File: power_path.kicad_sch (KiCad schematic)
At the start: 39 parts, among them J1 Battery, J2 USB_C_Receptacle_USB2.0_16P, SW1 MK-11C04-G013, U2 TPS631000DRLR, U3 TLV77018PDBVR, U4 TPS2116DRL, U5 USBLC6-2SC6, U6 USBLC6-2SC6, U7 BQ25302, U8 BQ27427YZFR

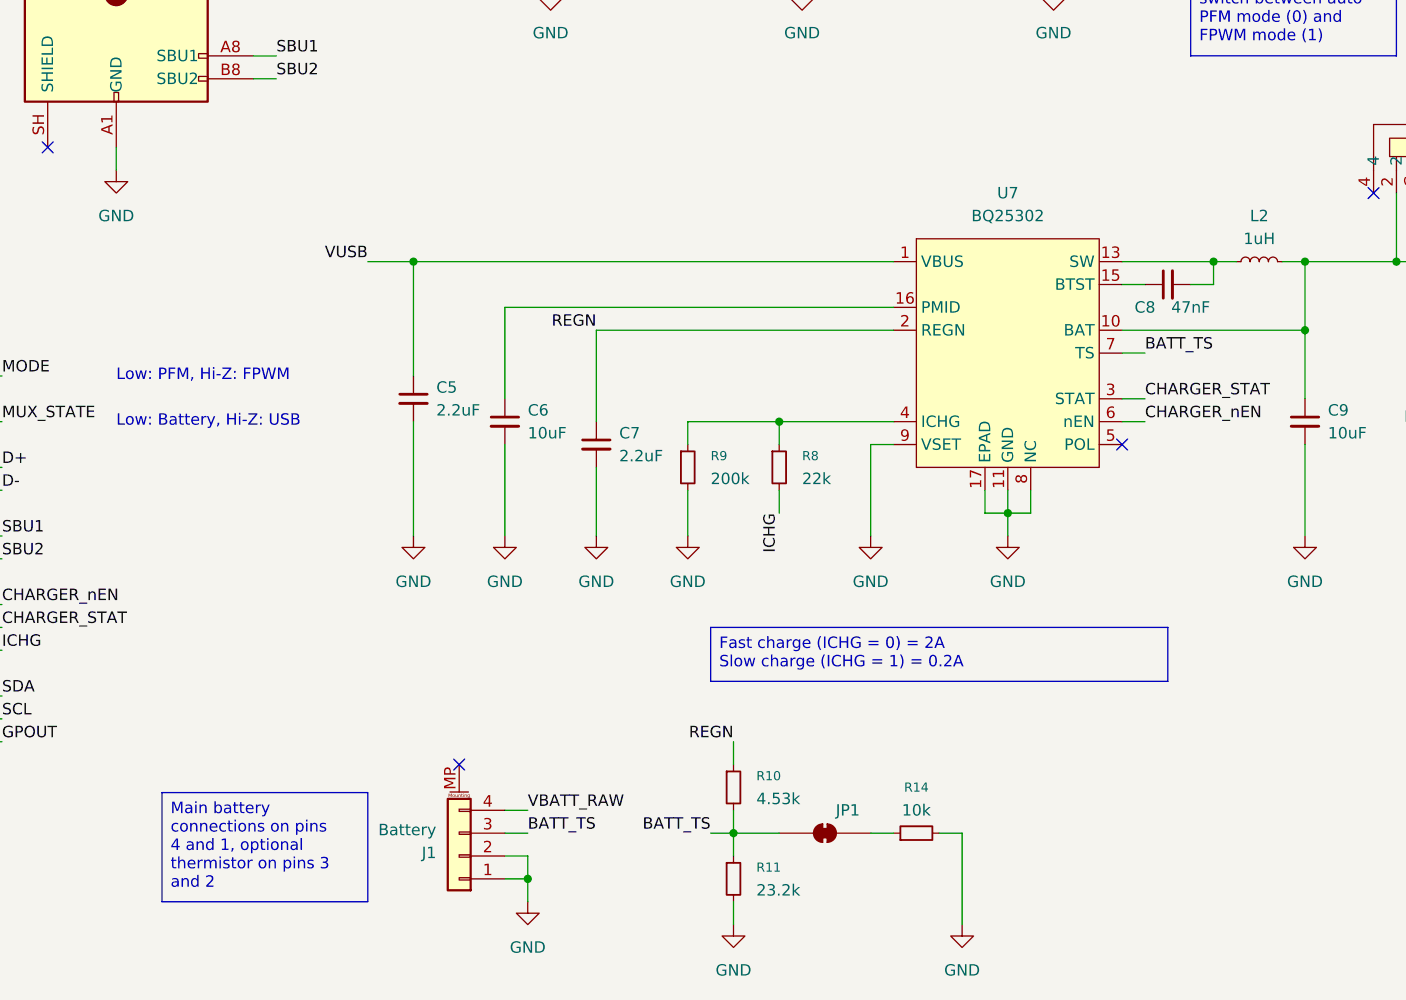
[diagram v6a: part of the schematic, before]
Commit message: add battery connector model and charge led
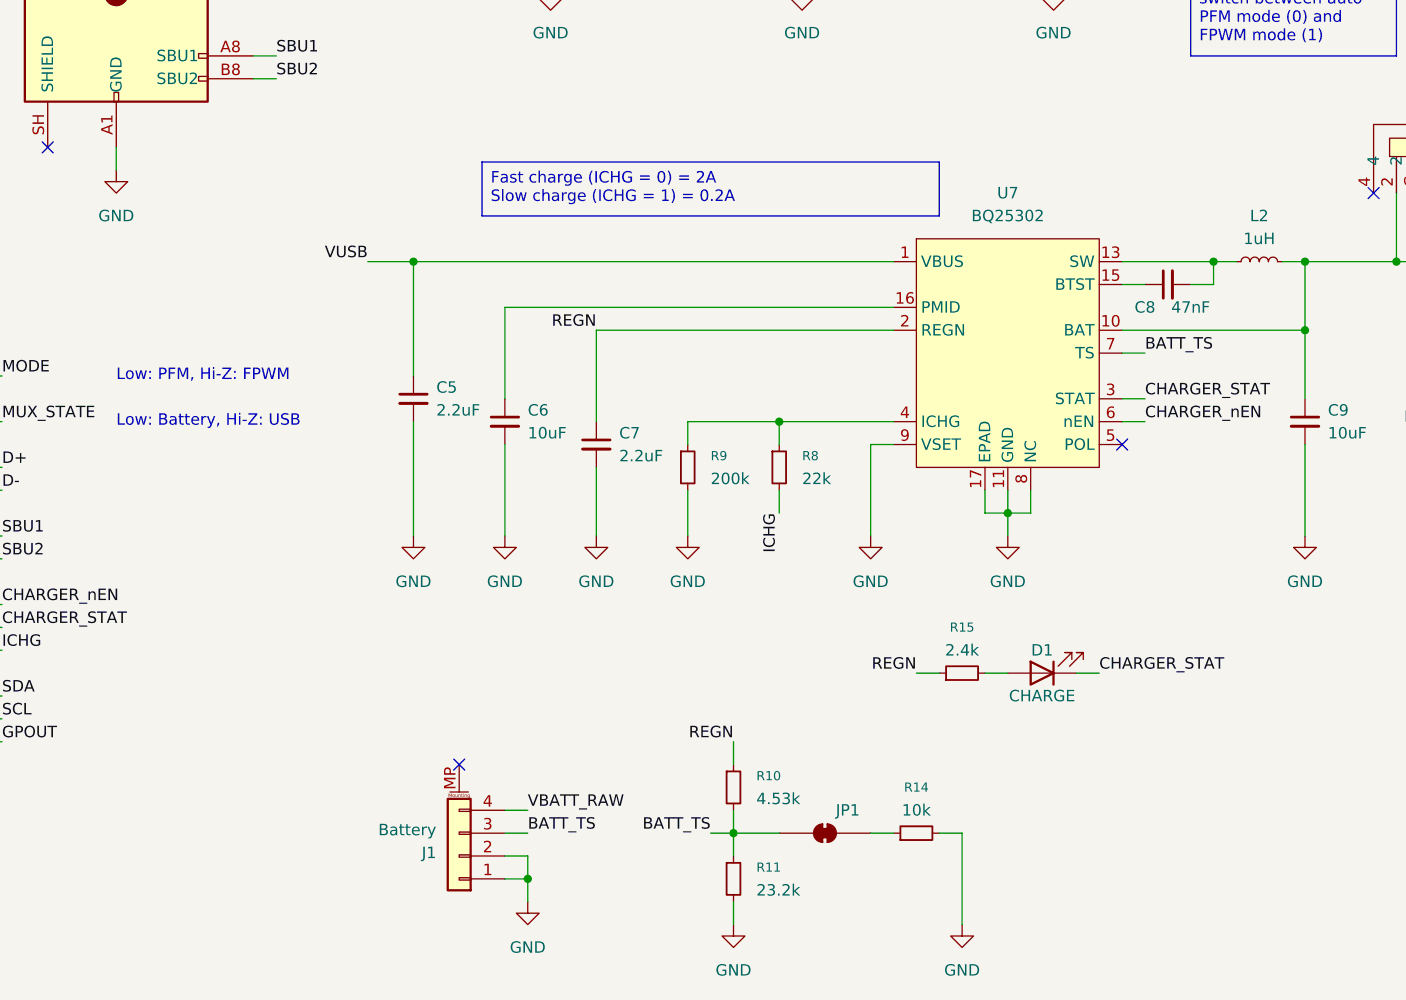
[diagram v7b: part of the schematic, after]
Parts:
- added D1: CHARGE, LED_SMD:LED_0402_1005Metric, symbol Device:LED
- added R15: 2.4k, Resistor_SMD:R_0402_1005Metric, symbol Device:R_Small
- J1: footprint (none) -> Connector_JST:JST_PH_S4B-PH-SM4-TB_1x04-1MP_P2.00mm_Horizontal; LCSC (none) -> C2763695
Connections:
- net CHARGER_STAT: now also D1.1 (K)
- net REGN: now also R15.1
- new net: D1.2 (A), R15.2

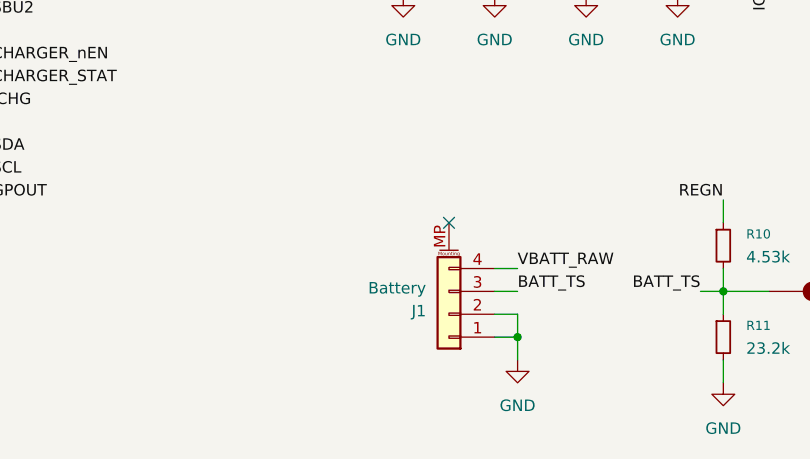
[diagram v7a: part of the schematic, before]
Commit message: replace battery connector with solder pads
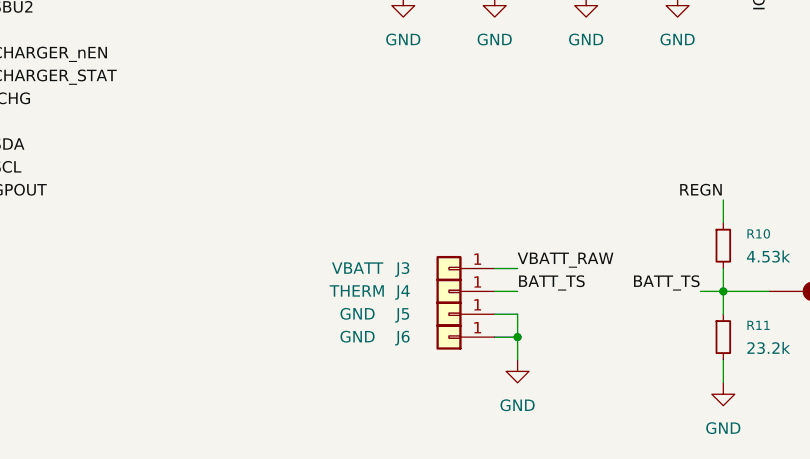
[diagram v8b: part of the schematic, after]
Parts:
- removed J1: Battery, Connector_JST:JST_PH_S4B-PH-SM4-TB_1x04-1MP_P2.00mm_Horizontal, symbol Connector_Generic_MountingPin:Conn_01x04_MountingPin
- added J3: VBATT, Connector_Wire:SolderWirePad_1x01_SMD_1x2mm, symbol Connector_Generic:Conn_01x01
- added J4: THERM, Connector_Wire:SolderWirePad_1x01_SMD_1x2mm, symbol Connector_Generic:Conn_01x01
- added J5, J6: GND, Connector_Wire:SolderWirePad_1x01_SMD_1x2mm, symbol Connector_Generic:Conn_01x01
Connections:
- net BATT_TS: now also J4.1 (Pin_1)
- net GND: now also J5.1 (Pin_1), J6.1 (Pin_1)
- net VBATT_RAW: now also J3.1 (Pin_1)
- no-connect marks 6 -> 5
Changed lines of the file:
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@@
 	)
 	(no_connect
-		(at 88.9 170.18)
-	)
-	(no_connect
 		(at 198.12 106.68)
 	)
@@
 	)
 	(symbol
+		(lib_id "Connector_Generic:Conn_01x01")
+		(at 88.9 177.8 180)
+		(unit 1)
+		(body_style 1)
+		(exclude_from_sim no)
+		(in_bom yes)
+		(on_board yes)
+		(in_pos_files yes)
+		(dnp no)
+		(property "Reference" "J4"
+			(at 83.82 177.8 0)
+			(show_name no)
+			(do_not_autoplace no)
+			(effects
+				(font
+					(size 1.27 1.27)
+				)
+			)
+		)
+		(property "Value" "THERM"
+			(at 78.74 177.8 0)
+			(show_name no)
+			(do_not_autoplace no)
+			(effects
+				(font
+					(size 1.27 1.27)
+				)
+			)
+		)
+		(property "Footprint" "Connector_Wire:SolderWirePad_1x01_SMD_1x2mm"
+			(at 88.9 177.8 0)
+			(hide yes)
+			(show_name no)
+			(do_not_autoplace no)
+			(effects
+				(font
+					(size 1.27 1.27)
+				)
+			)
+		)
+		(property "Datasheet" ""
+			(at 88.9 177.8 0)
+			(hide yes)
+			(show_name no)
+			(do_not_autoplace no)
+			(effects
+				(font
+					(size 1.27 1.27)
+				)
+			)
+		)
+		(property "Description" "Generic connector, single row, 01x01, script generated (kicad-library-utils/schlib/autogen/connector/)"
+			(at 88.9 177.8 0)
+			(hide yes)
+			(show_name no)
+			(do_not_autoplace no)
+			(effects
+				(font
+					(size 1.27 1.27)
+				)
+			)
+		)
+		(pin "1"
+		)
+		(instances
+			(project "pedal"
+				(path "/e2443317-b83f-4e66-ac79-3186c6d613f3/487ab5a8-1c1d-4a3e-8f62-a21afc38e9a3"
+					(reference "J4")
+					(unit 1)
+				)
+			)
+		)
+	)
+	(symbol
 		(lib_id "power:GND")
 		(at 96.52 185.42 0)
@@
 	)
 	(symbol
-		(lib_id "Connector_Generic_MountingPin:Conn_01x04_MountingPin")
-		(at 88.9 180.34 180)
+		(lib_id "Device:R_Small")
+		(at 71.12 71.12 90)
 		(unit 1)
 		(body_style 1)
@@
 		(in_pos_files yes)
 		(dnp no)
-		(fields_autoplaced yes)
-		(property "Reference" "J1"
-			(at 86.36 179.9845 0)
+		(property "Reference" "R7"
+			(at 68.58 73.66 90)
 			(show_name no)
 			(do_not_autoplace no)
 			(effects
 				(font
-					(size 1.27 1.27)
+					(size 1.016 1.016)
 				)
-				(justify left)
 			)
 		)
-		(property "Value" "Battery"
-			(at 86.36 177.4445 0)
+		(property "Value" "5.1k"
+			(at 73.66 73.66 90)
 			(show_name no)
 			(do_not_autoplace no)
@@
 					(size 1.27 1.27)
 				)
-				(justify left)
 			)
 		)
-		(property "Footprint" "Connector_JST:JST_PH_S4B-PH-SM4-TB_1x04-1MP_P2.00mm_Horizontal"
-			(at 88.9 180.34 0)
+		(property "Footprint" "Resistor_SMD:R_0402_1005Metric"
+			(at 71.12 71.12 0)
 			(hide yes)
 			(show_name no)
@@
 		)
 		(property "Datasheet" ""
-			(at 88.9 180.34 0)
+			(at 71.12 71.12 0)
 			(hide yes)
 			(show_name no)
@@
 			)
 		)
-		(property "Description" "Generic connectable mounting pin connector, single row, 01x04, script generated (kicad-library-utils/schlib/autogen/connector/)"
-			(at 88.9 180.34 0)
+		(property "Description" "Resistor, small symbol"
+			(at 71.12 71.12 0)
 			(hide yes)
 			(show_name no)
@@
 			)
 		)
-		(property "LCSC" "C2763695"
-			(at 88.9 180.34 0)
+		(property "LCSC" "C25905"
+			(at 71.12 71.12 0)
 			(hide yes)
 			(show_name no)
@@
 			)
 		)
-		(pin "2"
-		)
-		(pin "3"
-		)
-		(pin "MP"
-		)
-		(pin "4"
-		)
 		(pin "1"
 		)
+		(pin "2"
+		)
 		(instances
 			(project "pedal"
 				(path "/e2443317-b83f-4e66-ac79-3186c6d613f3/487ab5a8-1c1d-4a3e-8f62-a21afc38e9a3"
-					(reference "J1")
+					(reference "R7")
 					(unit 1)
 				)
@@
 	)
 	(symbol
-		(lib_id "Device:R_Small")
-		(at 71.12 71.12 90)
+		(lib_id "Connector_Generic:Conn_01x01")
+		(at 88.9 180.34 180)
 		(unit 1)
 		(body_style 1)
@@
 		(in_pos_files yes)
 		(dnp no)
-		(property "Reference" "R7"
-			(at 68.58 73.66 90)
-			(show_name no)
-			(do_not_autoplace no)
-			(effects
-				(font
-					(size 1.016 1.016)
-				)
-			)
-		)
-		(property "Value" "5.1k"
-			(at 73.66 73.66 90)
+		(property "Reference" "J5"
+			(at 83.82 180.34 0)
 			(show_name no)
 			(do_not_autoplace no)
@@
 			)
 		)
-		(property "Footprint" "Resistor_SMD:R_0402_1005Metric"
-			(at 71.12 71.12 0)
-			(hide yes)
+		(property "Value" "GND"
+			(at 78.74 180.34 0)
 			(show_name no)
 			(do_not_autoplace no)
@@
 			)
 		)
-		(property "Datasheet" ""
-			(at 71.12 71.12 0)
+		(property "Footprint" "Connector_Wire:SolderWirePad_1x01_SMD_1x2mm"
+			(at 88.9 180.34 0)
 			(hide yes)
 			(show_name no)
@@
 			)
 		)
-		(property "Description" "Resistor, small symbol"
-			(at 71.12 71.12 0)
+		(property "Datasheet" ""
+			(at 88.9 180.34 0)
 			(hide yes)
 			(show_name no)
@@
 			)
 		)
-		(property "LCSC" "C25905"
-			(at 71.12 71.12 0)
+		(property "Description" "Generic connector, single row, 01x01, script generated (kicad-library-utils/schlib/autogen/connector/)"
+			(at 88.9 180.34 0)
 			(hide yes)
 			(show_name no)
@@
 		(pin "1"
 		)
-		(pin "2"
-		)
 		(instances
 			(project "pedal"
 				(path "/e2443317-b83f-4e66-ac79-3186c6d613f3/487ab5a8-1c1d-4a3e-8f62-a21afc38e9a3"
-					(reference "R7")
+					(reference "J5")
 					(unit 1)
 				)
@@
 	)
 	(symbol
+		(lib_id "Connector_Generic:Conn_01x01")
+		(at 88.9 182.88 180)
+		(unit 1)
+		(body_style 1)
+		(exclude_from_sim no)
+		(in_bom yes)
+		(on_board yes)
+		(in_pos_files yes)
+		(dnp no)
+		(property "Reference" "J6"
+			(at 83.82 182.88 0)
+			(show_name no)
+			(do_not_autoplace no)
+			(effects
+				(font
+					(size 1.27 1.27)
+				)
+			)
+		)
+		(property "Value" "GND"
+			(at 78.74 182.88 0)
+			(show_name no)
+			(do_not_autoplace no)
+			(effects
+				(font
+					(size 1.27 1.27)
+				)
+			)
+		)
+		(property "Footprint" "Connector_Wire:SolderWirePad_1x01_SMD_1x2mm"
+			(at 88.9 182.88 0)
+			(hide yes)
+			(show_name no)
+			(do_not_autoplace no)
+			(effects
+				(font
+					(size 1.27 1.27)
+				)
+			)
+		)
+		(property "Datasheet" ""
+			(at 88.9 182.88 0)
+			(hide yes)
+			(show_name no)
+			(do_not_autoplace no)
+			(effects
+				(font
+					(size 1.27 1.27)
+				)
+			)
+		)
+		(property "Description" "Generic connector, single row, 01x01, script generated (kicad-library-utils/schlib/autogen/connector/)"
+			(at 88.9 182.88 0)
+			(hide yes)
+			(show_name no)
+			(do_not_autoplace no)
+			(effects
+				(font
+					(size 1.27 1.27)
+				)
+			)
+		)
+		(pin "1"
+		)
+		(instances
+			(project "pedal"
+				(path "/e2443317-b83f-4e66-ac79-3186c6d613f3/487ab5a8-1c1d-4a3e-8f62-a21afc38e9a3"
+					(reference "J6")
+					(unit 1)
+				)
+			)
+		)
+	)
+	(symbol
 		(lib_id "Device:Battery_Cell")
 		(at 208.28 132.08 0)
@@
 					(unit 1)
 				)
+			)
+		)
+	)
+	(symbol
+		(lib_id "Connector_Generic:Conn_01x01")
+		(at 88.9 175.26 180)
+		(unit 1)
+		(body_style 1)
+		(exclude_from_sim no)
+		(in_bom yes)
+		(on_board yes)
+		(in_pos_files yes)
+		(dnp no)
+		(property "Reference" "J3"
+			(at 83.82 175.26 0)
+			(show_name no)
+			(do_not_autoplace no)
+			(effects
+				(font
+					(size 1.27 1.27)
+				)
+			)
+		)
+		(property "Value" "VBATT"
+			(at 78.74 175.26 0)
+			(show_name no)
+			(do_not_autoplace no)
+			(effects
+				(font
+					(size 1.27 1.27)
+				)
+			)
+		)
+		(property "Footprint" "Connector_Wire:SolderWirePad_1x01_SMD_1x2mm"
+			(at 88.9 175.26 0)
+			(hide yes)
+			(show_name no)
+			(do_not_autoplace no)
+			(effects
+				(font
+					(size 1.27 1.27)
+				)
+			)
+		)
+		(property "Datasheet" ""
+			(at 88.9 175.26 0)
+			(hide yes)
+			(show_name no)
+			(do_not_autoplace no)
+			(effects
+				(font
+					(size 1.27 1.27)
+				)
+			)
+		)
+		(property "Description" "Generic connector, single row, 01x01, script generated (kicad-library-utils/schlib/autogen/connector/)"
+			(at 88.9 175.26 0)
+			(hide yes)
+			(show_name no)
+			(do_not_autoplace no)
+			(effects
+				(font
+					(size 1.27 1.27)
+				)
+			)
+		)
+		(pin "1"
+		)
+		(instances
+			(project "pedal"
+				(path "/e2443317-b83f-4e66-ac79-3186c6d613f3/487ab5a8-1c1d-4a3e-8f62-a21afc38e9a3"
+					(reference "J3")
+					(unit 1)
+				)
